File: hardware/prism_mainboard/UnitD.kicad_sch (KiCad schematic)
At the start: 1 part, among them U1 XC7Z010-1CLG400C

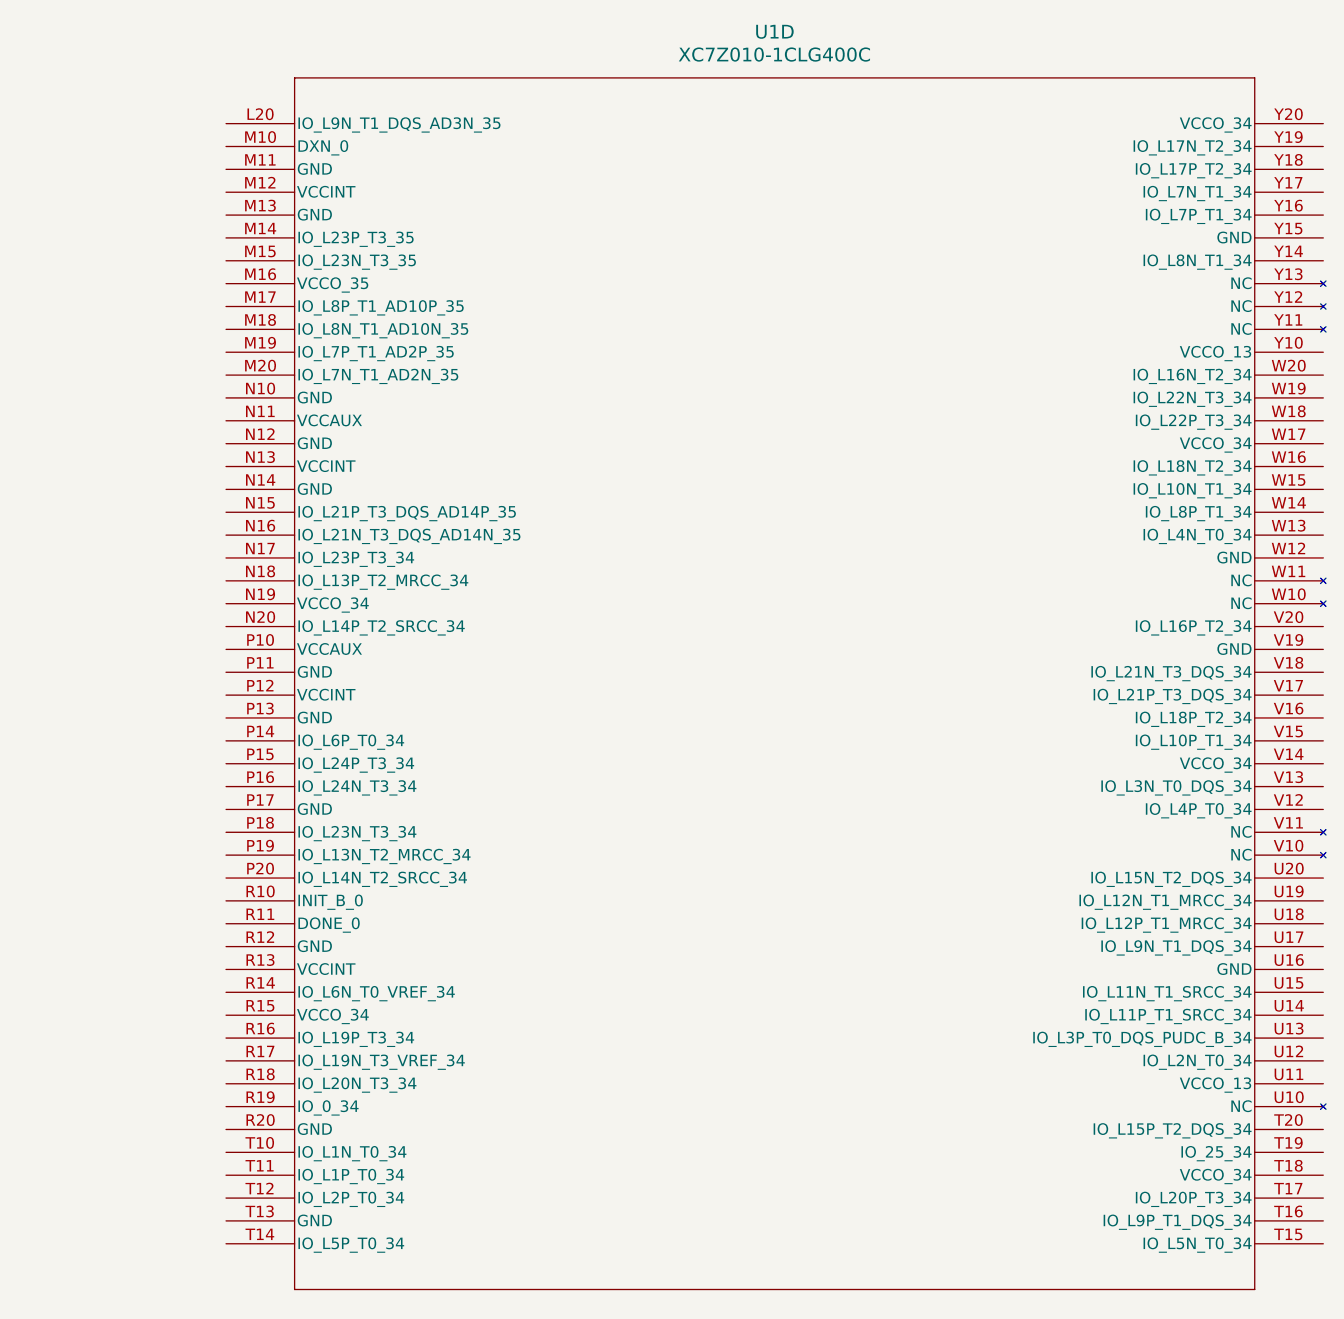
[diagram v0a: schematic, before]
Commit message: Mainboard Updates
Started a lot of the basic schematic nets like GND and Power nets. Major Change: Decided on using the XC7Z015-1CLG485I instead of the 7010 or 7020 due to the ability to use HDMI interfaces with an adapter and more LUTs. Updated schematic symbols and footprints accordingly. Added Memory, Encoder, MicroSD schematics. Added LimeSDR footprints as well. Will Try to add Power to the entire board next.
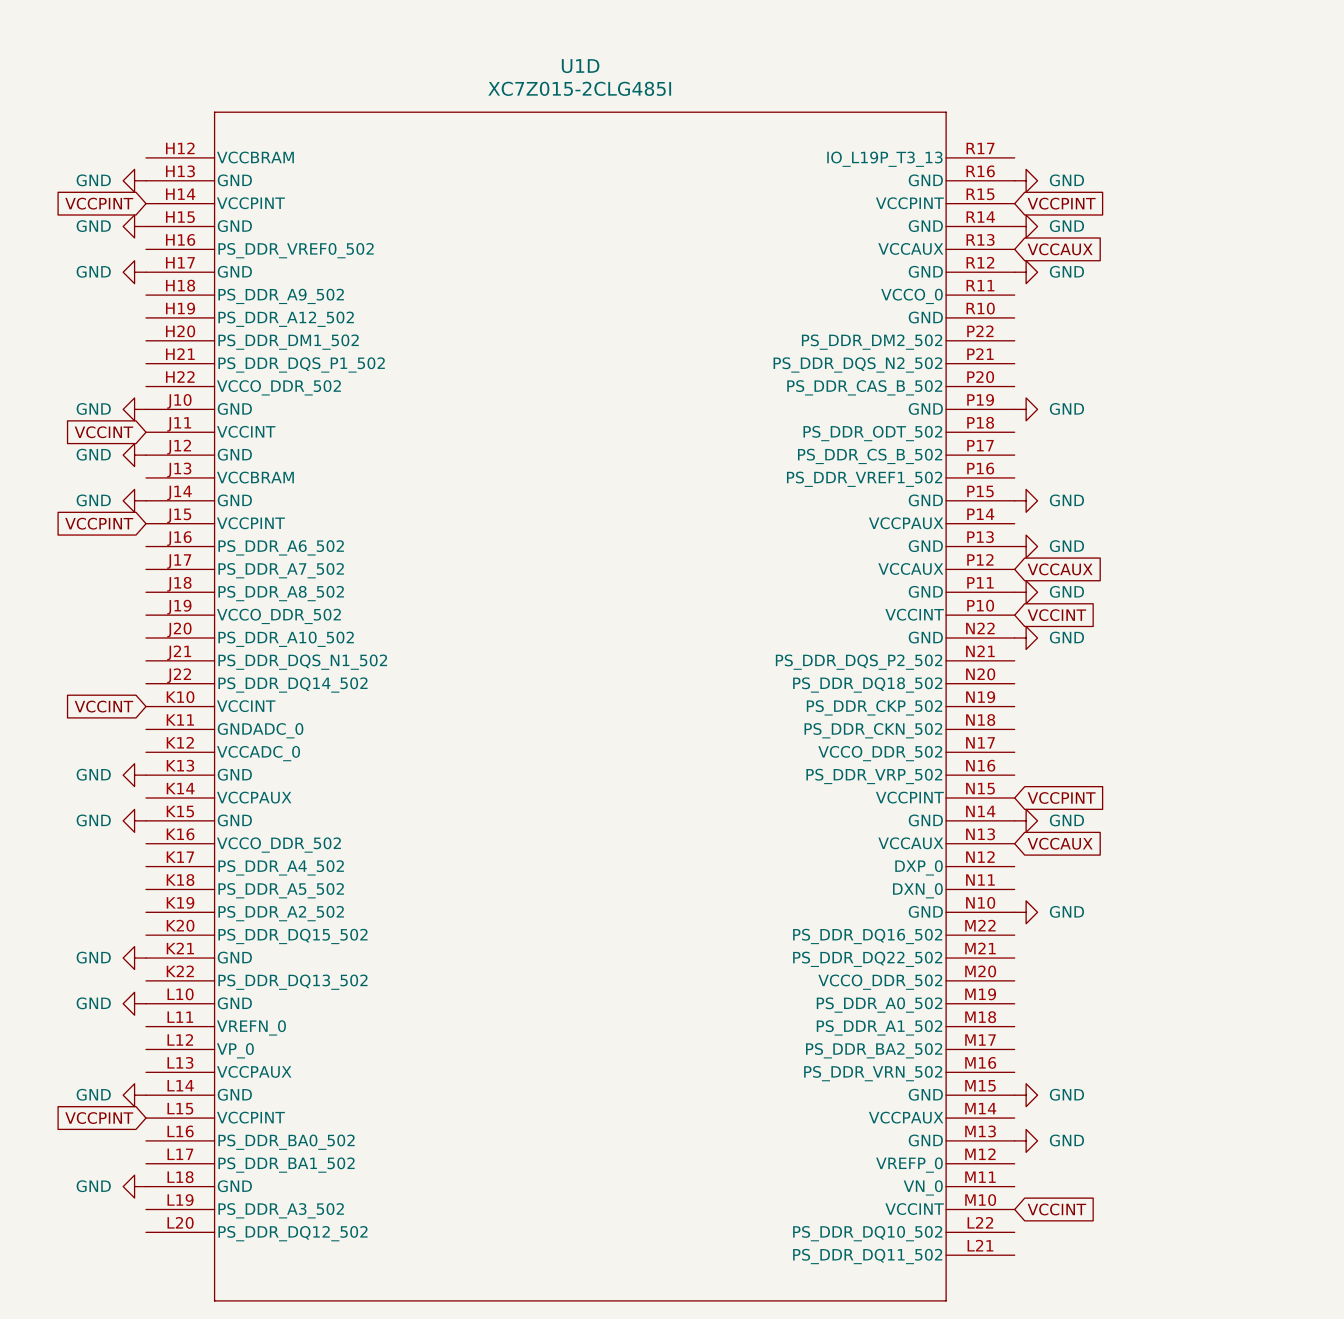
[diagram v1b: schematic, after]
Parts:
- removed U1: XC7Z010-1CLG400C, XC7Z010-1CLG400C:CLG400_XIL, symbol XC7Z010-1CLG400C:XC7Z010-1CLG400C
- added U1: XC7Z015-2CLG485I, CLG485_XIL, symbol XC7Z015-CLG485:XC7Z015-2CLG485I
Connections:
- new net GND: U1.H13 (GND), U1.H15 (GND), U1.H17 (GND), U1.J10 (GND), U1.J12 (GND), U1.J14 (GND), U1.K13 (GND), U1.K15 (GND), U1.K21 (GND), U1.L10 (GND), U1.L14 (GND), U1.L18 (GND), U1.M13 (GND), U1.M15 (GND), U1.N10 (GND), U1.N14 (GND), U1.N22 (GND), U1.P11 (GND), U1.P13 (GND), U1.P15 (GND), U1.P19 (GND), U1.R12 (GND), U1.R14 (GND), U1.R16 (GND)
- new net VCCAUX: U1.N13 (VCCAUX), U1.P12 (VCCAUX), U1.R13 (VCCAUX)
- new net VCCINT: U1.J11 (VCCINT), U1.K10 (VCCINT), U1.M10 (VCCINT), U1.P10 (VCCINT)
- new net VCCPINT: U1.H14 (VCCPINT), U1.J15 (VCCPINT), U1.L15 (VCCPINT), U1.N15 (VCCPINT), U1.R15 (VCCPINT)

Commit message: Schematic Updates
Updated the DDR3 DRAM to 4Gb, added a lot of nets and started updating the power and decoupling components. Updated .gitignore to avoid .mkv files.
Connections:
- net GND: now also U1.K11 (GNDADC_0)
- net VCCBRAM: now reaches U1.H12 (VCCBRAM)
- net VCCBRAM: now also U1.J13 (VCCBRAM)
- net VCCO_DDR: now reaches U1.H22 (VCCO_DDR_502)
- net VCCO_DDR: now also U1.J19 (VCCO_DDR_502), U1.K16 (VCCO_DDR_502), U1.M20 (VCCO_DDR_502), U1.N17 (VCCO_DDR_502)
- net VCCPAUX: now reaches U1.K14 (VCCPAUX)
- net VCCPAUX: now also U1.L13 (VCCPAUX), U1.M14 (VCCPAUX), U1.P14 (VCCPAUX)
- net VCCO_0: now reaches U1.R11 (VCCO_0)
